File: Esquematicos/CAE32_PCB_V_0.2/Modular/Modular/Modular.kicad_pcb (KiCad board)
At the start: 4 copper layers, 23 parts, among them J1 Steering Wheel Feedback, J2 Pedals, J3 Shifter, J4 Accessory_2, J5 Accessory_1, J6 Conn_01x04, J7 Screw_Terminal_01x02, P1 USB_C_Plug_USB2.0, U1 ESP32-S3-WROOM-1, U3 LDL1117

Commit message: Actualización de README
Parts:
- added D3: LED, LED_SMD:LED_0805_2012Metric_Pad1.15x1.40mm_HandSolder, F.Cu at (120.2, 123.5)
- moved J2 100.0 mm to (86.0, 125.5), turned to -90 degrees
- moved F1 86.4 mm to (95.3, 126.3), turned to -90 degrees
- moved C5 76.5 mm to (100.5, 132.1), turned to -90 degrees
- moved U2 72.9 mm to (103.5, 126.5), turned to 0 degrees
- moved C6 67.9 mm to (106.5, 132.1), turned to -90 degrees
- moved BOOT1 64.1 mm to (102.0, 110.0), turned to 180 degrees
- moved D1 46.1 mm to (94.0, 114.0)
- moved P1 45.0 mm to (87.0, 115.5)
- moved D2 44.4 mm to (94.0, 117.0)
- moved U1 26.5 mm to (140.0, 122.0)
- moved C4 25.6 mm to (120.2, 117.1)
- moved R1 25.6 mm to (127.3, 117.1)
- moved R2 25.6 mm to (123.7, 117.1)
- moved J7 25.5 mm to (95.6, 144.9), turned to 180 degrees
- moved C1 25.1 mm to (127.3, 112.5)
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- renumbered C7 to C1, C8 to C2, C5 to C3, C6 to C4, C2 to C5, C4 to C6, J6 to J1, J7 to J2, J5 to J3, J1 to J4, J2 to J5, J3 to J6, J4 to J7, U3 to U2
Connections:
- U1 pad 17: /CS_PDL -> /CS_SWF
- U1 pad 18: /CS_SWF -> /CS_PDL
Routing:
- net /MISO: track 429.7 -> 148.4 mm, vias 1 -> 9
- net +5V: track 274.4 -> 159.4 mm, vias 0 -> 1
- net GNDREF: track 67.6 -> 2.73 mm, vias 31 -> 0
- net /SCLK: track 222.0 -> 159.0 mm
- net /MOSI: track 188.7 -> 134.4 mm
- net /CS_SWF: track 74.2 -> 27.7 mm, vias 3 -> 0
- net /BOOT: track 19.2 -> 64.4 mm
- net /CS_SHIF: track 50.0 -> 26.5 mm, vias 2 -> 0
- net /CS_A1: track 35.4 -> 12.5 mm, vias 3 -> 0
- net /CS_PDL: track 39.5 -> 19.8 mm, vias 1 -> 0
- net /CS_A2: track 39.4 -> 50.3 mm, vias 1 -> 0
- net /D+: track 47.9 -> 56.9 mm
- net /D-: track 45.8 -> 54.6 mm
- net +3.3V: track 21.0 -> 26.7 mm, vias 0 -> 4
- net /TX_ESP: track 15.4 -> 20.2 mm, vias 1 -> 0
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- added copper zone on B.Cu, net +3.3V
- added copper zone on F.Cu, net GNDREF
- removed copper zone on F.Cu, net +3.3V
- removed copper zone on B.Cu, net GNDREF
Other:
- board outline added: 93.8 x 56.5 mm
- board text added: "3v3"
- board text added: "5V"
- board text added: "GND"
- board text added: "RX"
- board text added: "TX"

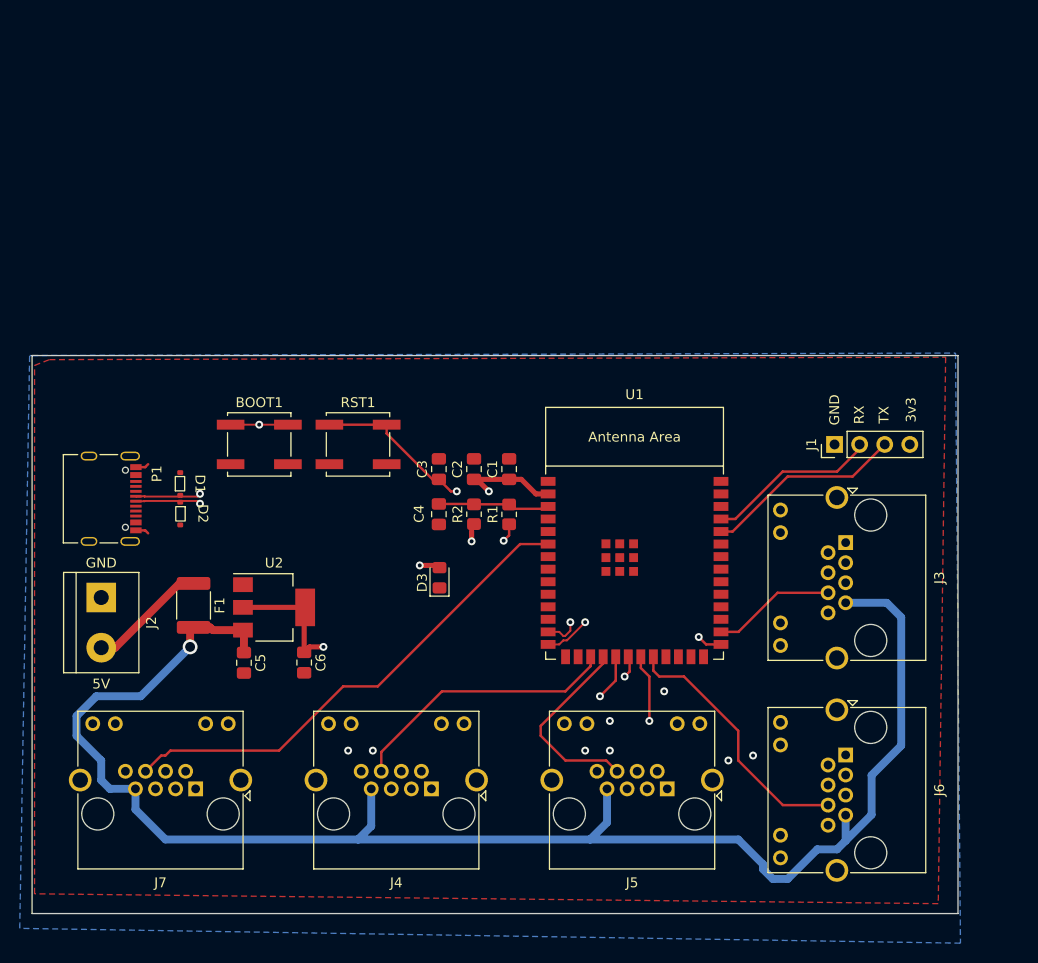
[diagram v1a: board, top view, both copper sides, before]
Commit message: Actualización de Gerbers e indicador de status de conexión
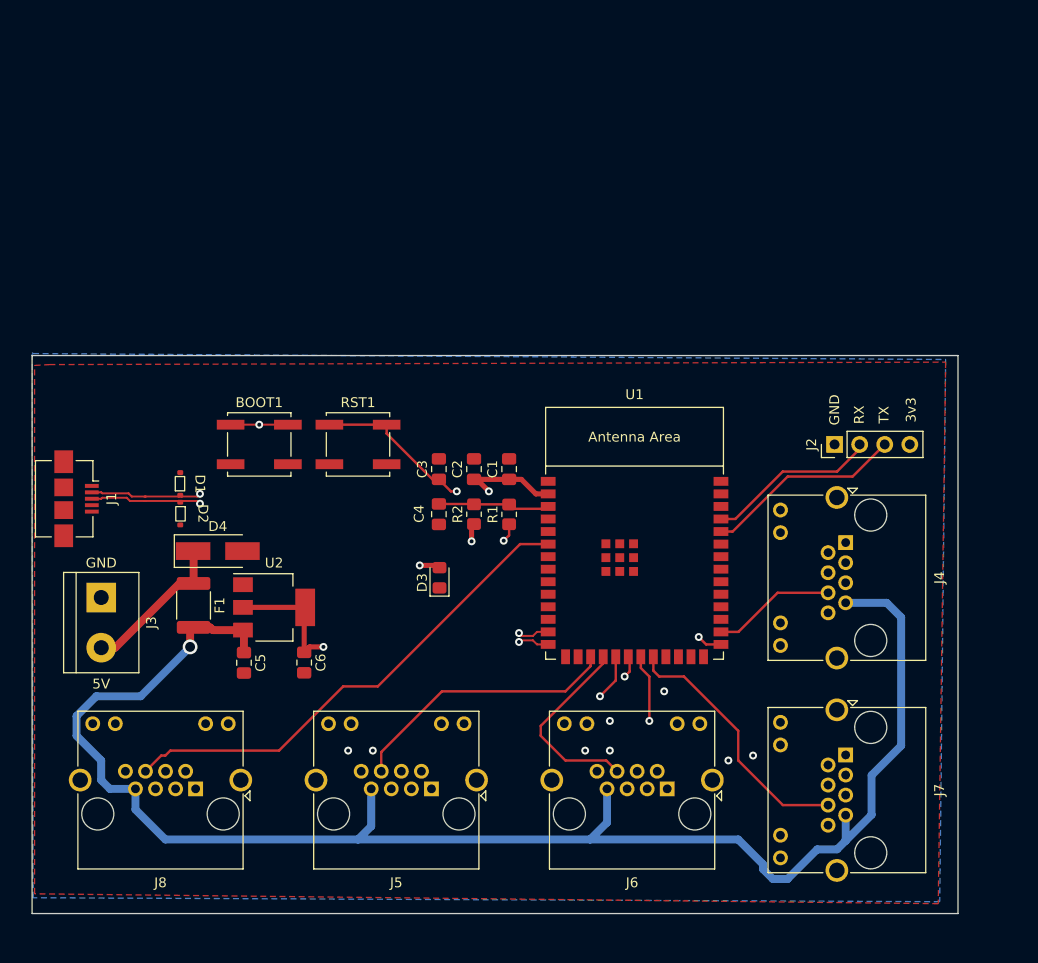
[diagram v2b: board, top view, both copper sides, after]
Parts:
- removed P1: USB_C_Plug_USB2.0, Connector_USB:USB_C_Receptacle_Palconn_UTC16-G
- added D4: D_Schottky, Diode_SMD:D_SMA_Handsoldering, F.Cu at (97.8, 120.8)
- added J1: USB_OTG, Connector_USB:USB_Micro-B_Amphenol_10104110_Horizontal, F.Cu at (83.5, 115.5)
- renumbered J1 to J2, J2 to J3, J3 to J4, J4 to J5, J5 to J6, J6 to J7, J7 to J8
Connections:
- D1 pad 1: /D+ -> /D-
- D2 pad 1: /D- -> /D+
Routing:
- net /D+: track 56.9 -> 53.3 mm
- net Net-(J3-Pad2): track 12.0 -> 15.3 mm
- net GNDREF: track 2.73 -> 0.00 mm
- net /D-: track 54.6 -> 53.3 mm
